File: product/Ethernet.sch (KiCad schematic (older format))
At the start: 25 parts, among them J3 RJ45_Amphenol_RJMG1BD3B8K1ANR, U2 LAN8720A

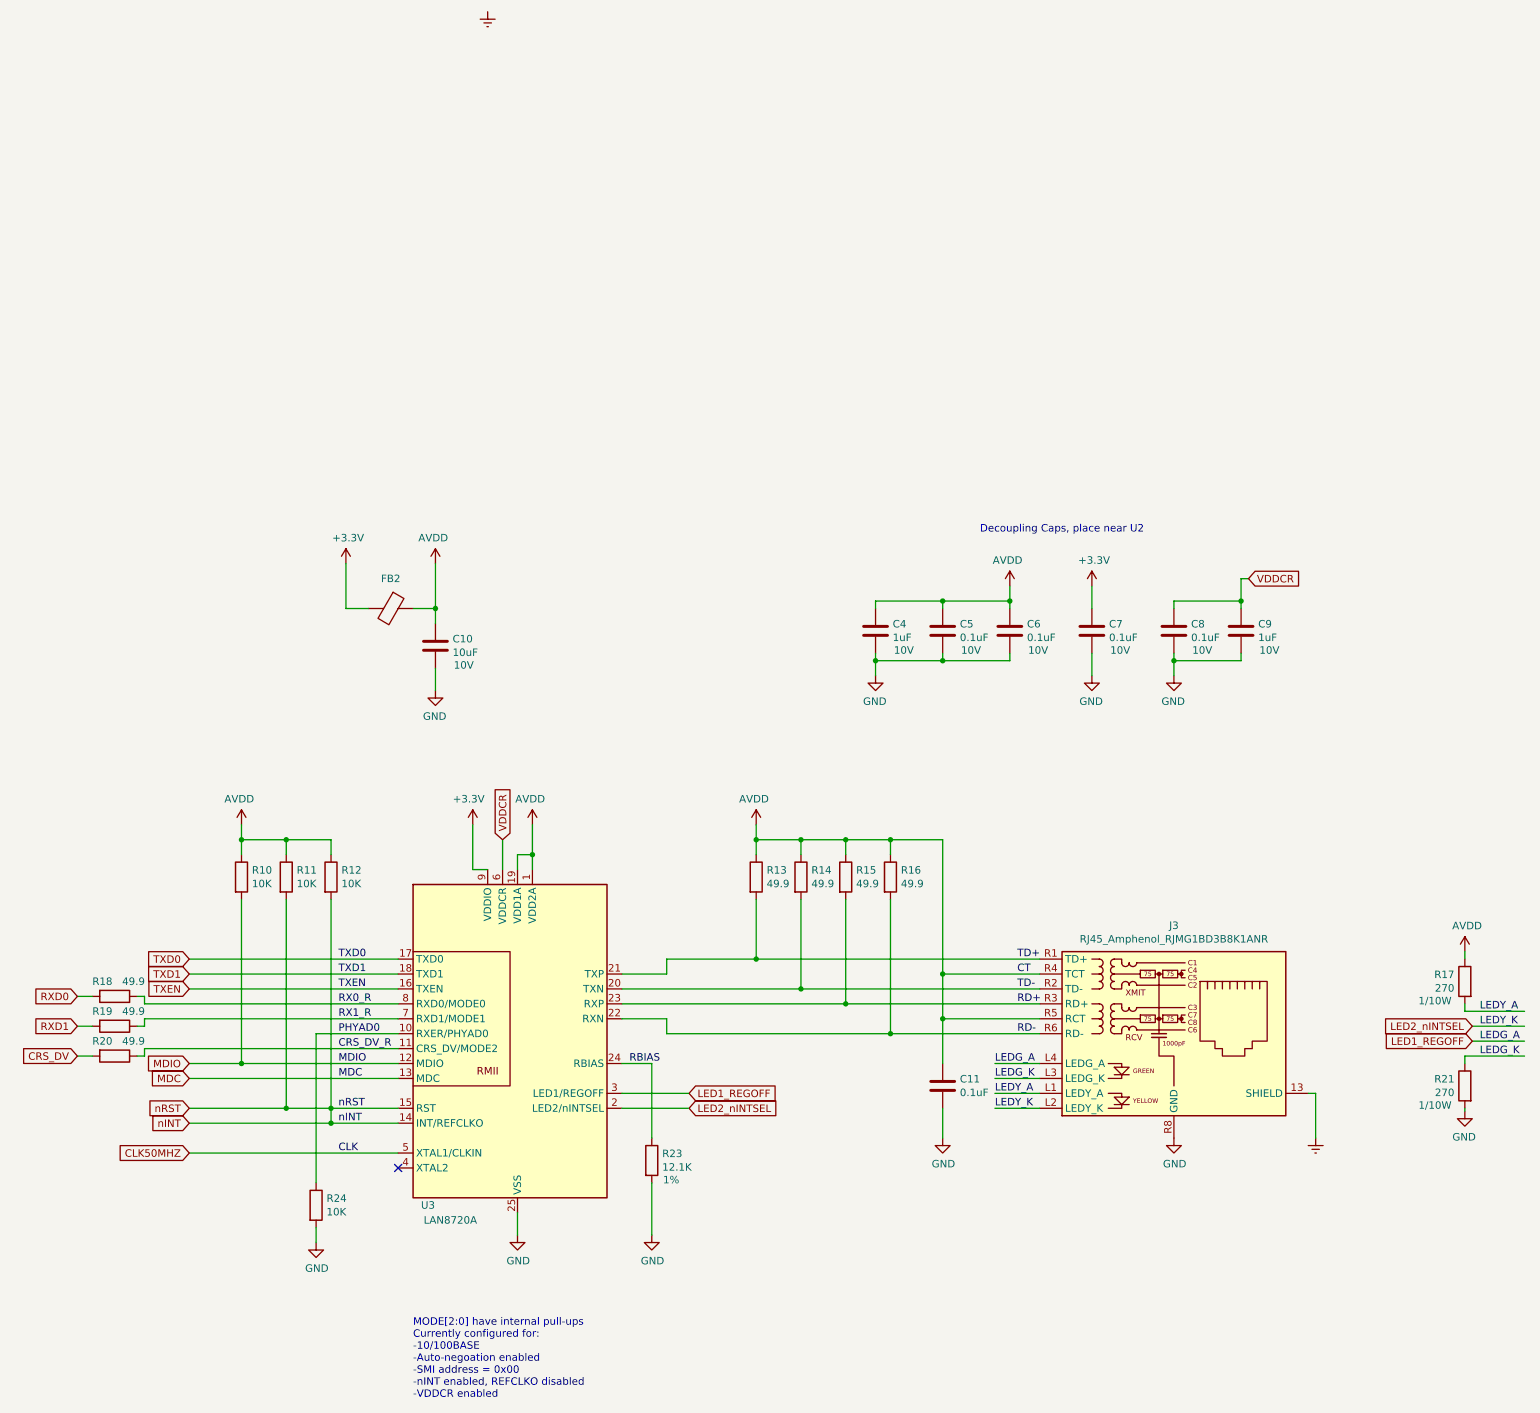
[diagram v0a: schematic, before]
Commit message: Added LCSC part numbers, and tweaked a few part footprints
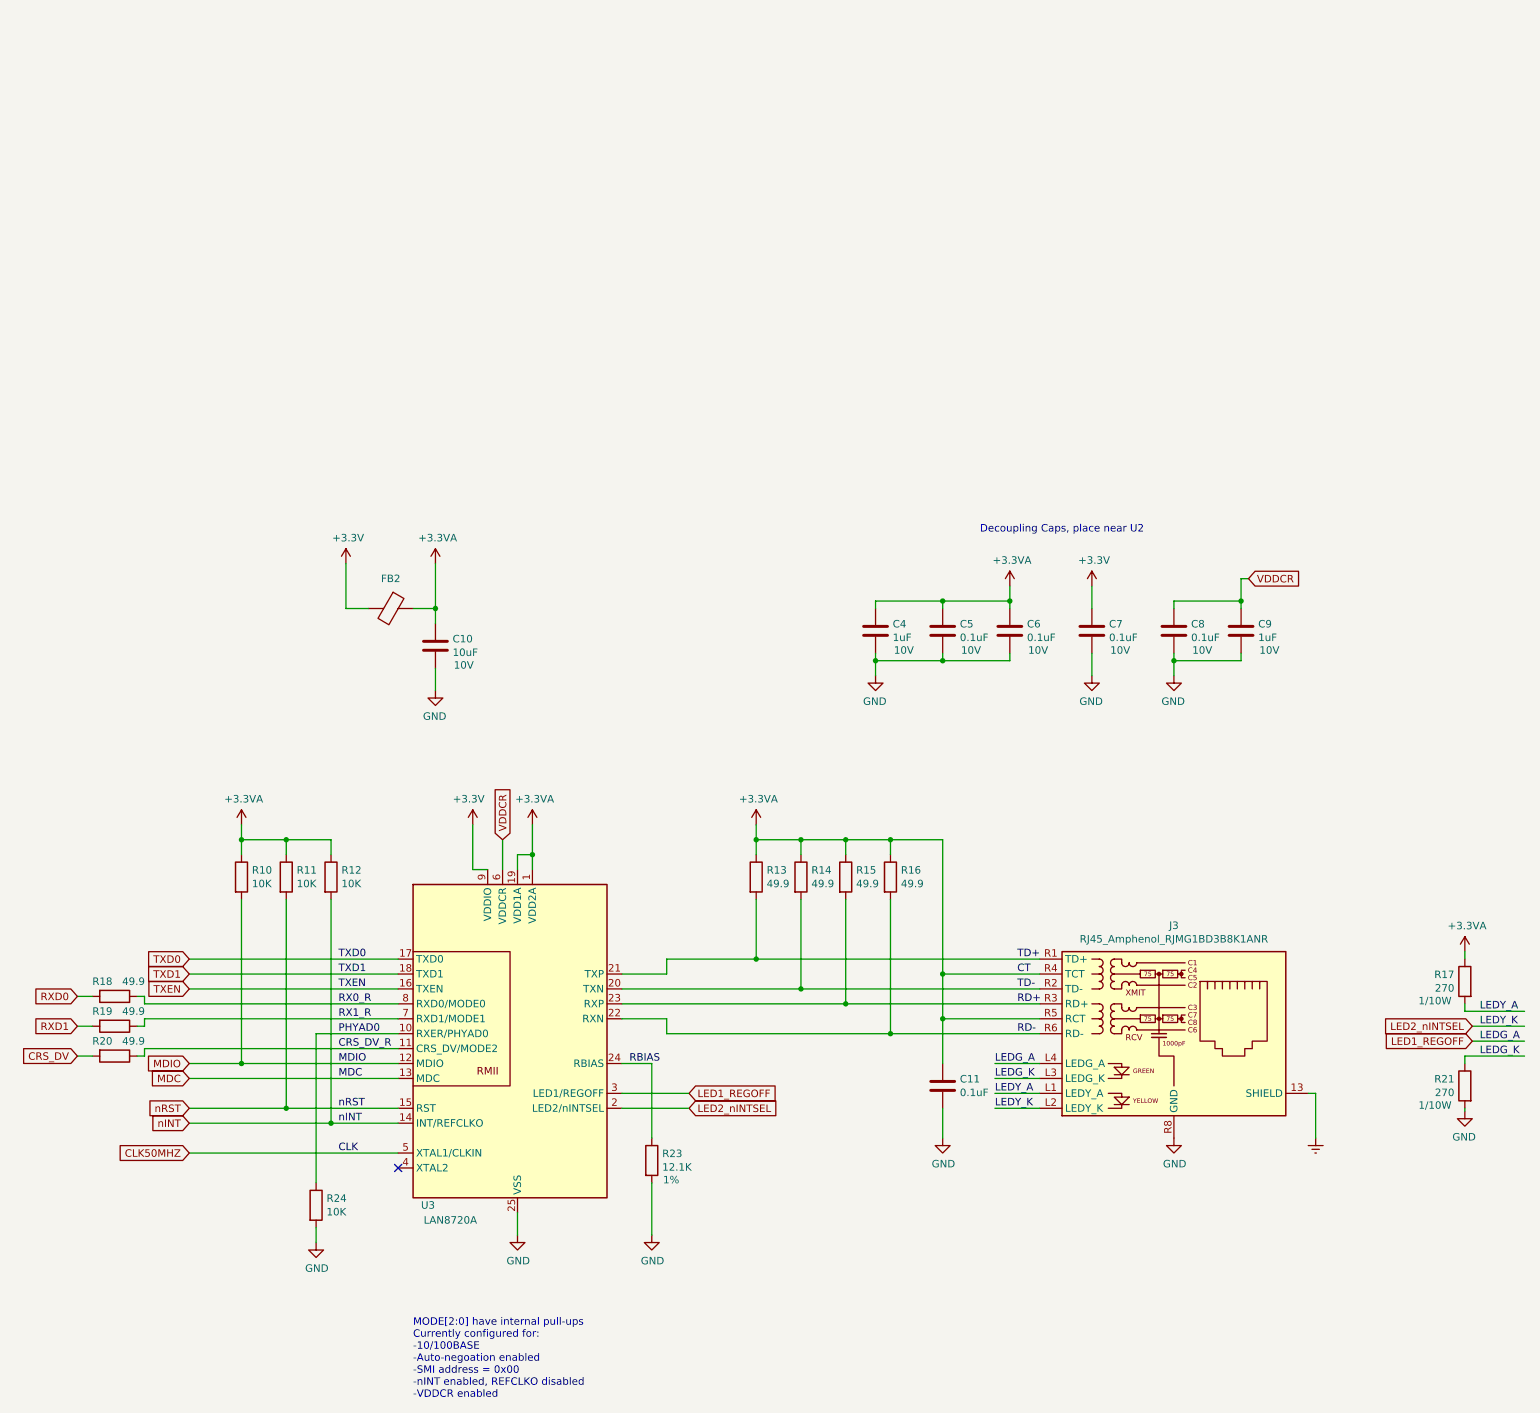
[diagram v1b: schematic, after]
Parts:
- C10, C5, C7, C8, C9: LCSC (none) -> C1525; LCSC Part Number (none) -> C1525
- C11, C6: LCSC (none) -> C52923; LCSC Part Number (none) -> C52923
- C4: footprint Capacitor_SMD:C_0603_1608Metric -> Capacitor_SMD:C_0805_2012Metric; LCSC (none) -> C19702; LCSC Part Number (none) -> C19702
- FB2: footprint Inductor_SMD:L_0603_1608Metric -> Inductor_SMD:L_0805_2012Metric; LCSC (none) -> C1015; LCSC Part Number (none) -> C1015
- R10, R11, R5, R6, R7, R8, R9: LCSC (none) -> C25120; LCSC Part Number (none) -> C25120
- R13: Extended Part (none) -> X; LCSC (none) -> C25852; LCSC Part Number (none) -> C25852
- R14, R2, R3, R4: LCSC (none) -> C25744; LCSC Part Number (none) -> C25744
- R15, R16: footprint Resistor_SMD:R_0402_1005Metric -> Resistor_SMD:R_0603_1608Metric; LCSC (none) -> C22966; LCSC Part Number (none) -> C22966
- U2: Extended Part (none) -> X; LCSC (none) -> C45223; LCSC Part Number (none) -> C45223
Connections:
- net labels added: +3.3VA
- net labels removed: AVDD
- wire segments 124 -> 122
